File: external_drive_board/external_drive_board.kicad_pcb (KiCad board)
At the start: 2 copper layers, 90 x 90 mm, 26 parts, among them J1 MD-90SM, J2 MD-90SM, J3 Conn_02x17_Odd_Even, J4 Conn_01x04, J5 Conn_01x02, J6 Conn_01x02, J7 Conn_01x02, SW1 SW_DIP_x04, U1 74LS125, U2 74LS85, U3 74LS595, U4 74LS165, U5 74LS04

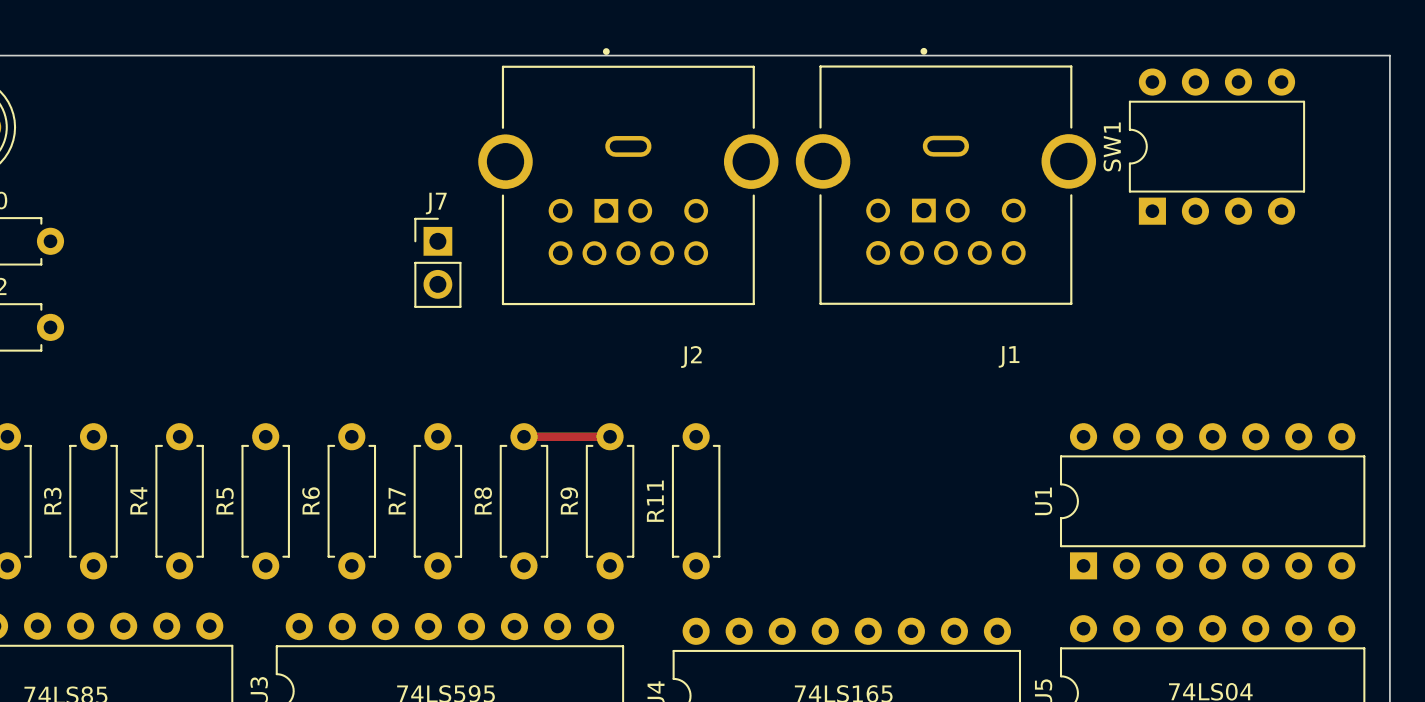
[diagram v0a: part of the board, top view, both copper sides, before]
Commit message: add dipsw reading to M1565 via spare bit
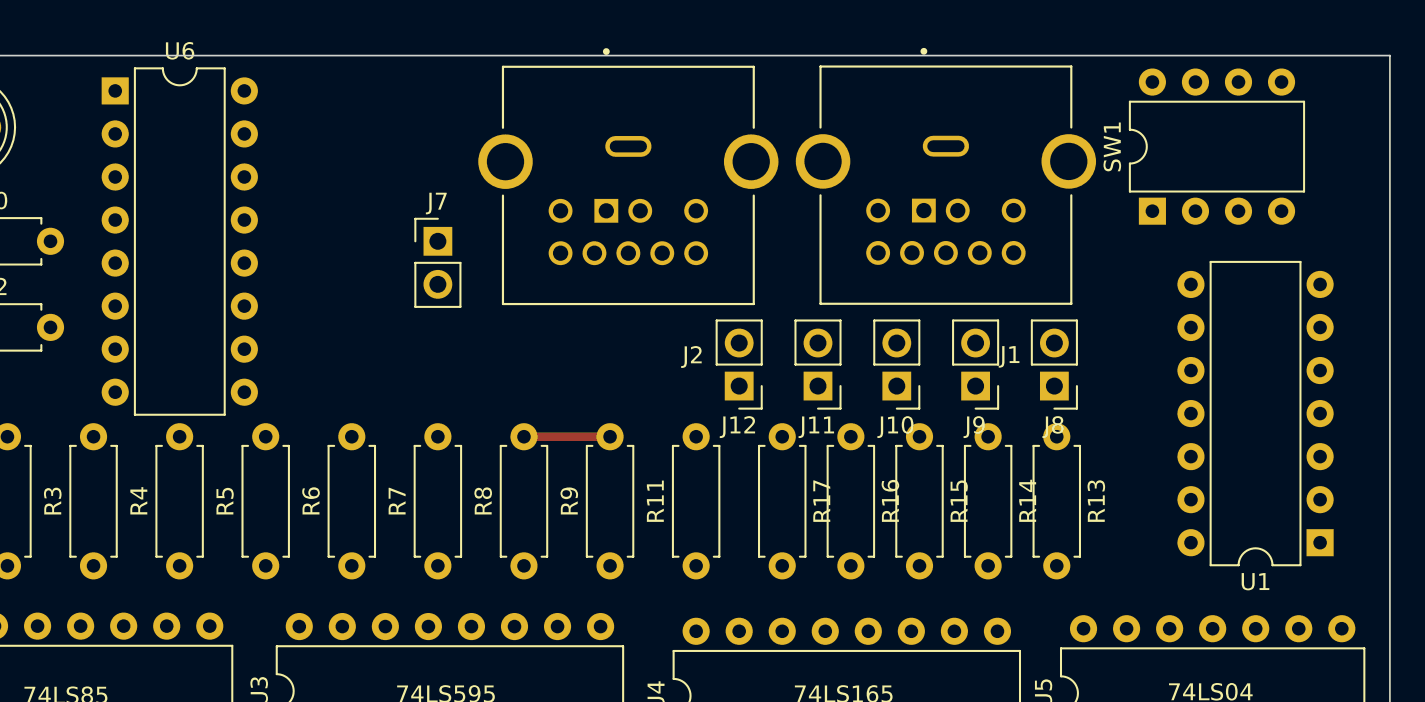
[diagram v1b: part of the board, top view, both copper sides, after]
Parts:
- added J10: RESERVED2, Connector_PinHeader_2.54mm:PinHeader_1x02_P2.54mm_Vertical, F.Cu at (110.9, 69.5)
- added J11: HD Drive, Connector_PinHeader_2.54mm:PinHeader_1x02_P2.54mm_Vertical, F.Cu at (106.2, 69.5)
- added J12: 5.25" Drive, Connector_PinHeader_2.54mm:PinHeader_1x02_P2.54mm_Vertical, F.Cu at (101.6, 69.5)
- added J8: RESERVED1, Connector_PinHeader_2.54mm:PinHeader_1x02_P2.54mm_Vertical, F.Cu at (120.2, 69.5)
- added J9: RESERVED3, Connector_PinHeader_2.54mm:PinHeader_1x02_P2.54mm_Vertical, F.Cu at (115.5, 69.5)
- added R13: 3K3, Resistor_THT:R_Axial_DIN0207_L6.3mm_D2.5mm_P7.62mm_Horizontal, F.Cu at (120.3, 72.5)
- added R14: 3K3, Resistor_THT:R_Axial_DIN0207_L6.3mm_D2.5mm_P7.62mm_Horizontal, F.Cu at (116.3, 72.5)
- added R15: 3K3, Resistor_THT:R_Axial_DIN0207_L6.3mm_D2.5mm_P7.62mm_Horizontal, F.Cu at (112.2, 72.5)
- added R16: 3K3, Resistor_THT:R_Axial_DIN0207_L6.3mm_D2.5mm_P7.62mm_Horizontal, F.Cu at (108.2, 72.5)
- added R17: 3K3, Resistor_THT:R_Axial_DIN0207_L6.3mm_D2.5mm_P7.62mm_Horizontal, F.Cu at (104.1, 72.5)
- added U6: 74LS165, Package_DIP:DIP-16_W7.62mm, F.Cu at (64.8, 52.1)
- moved U1 14.0 mm to (135.9, 78.7), turned to 180 degrees
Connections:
- U4 pad 6: SPR_SPARE -> M1565_DAT

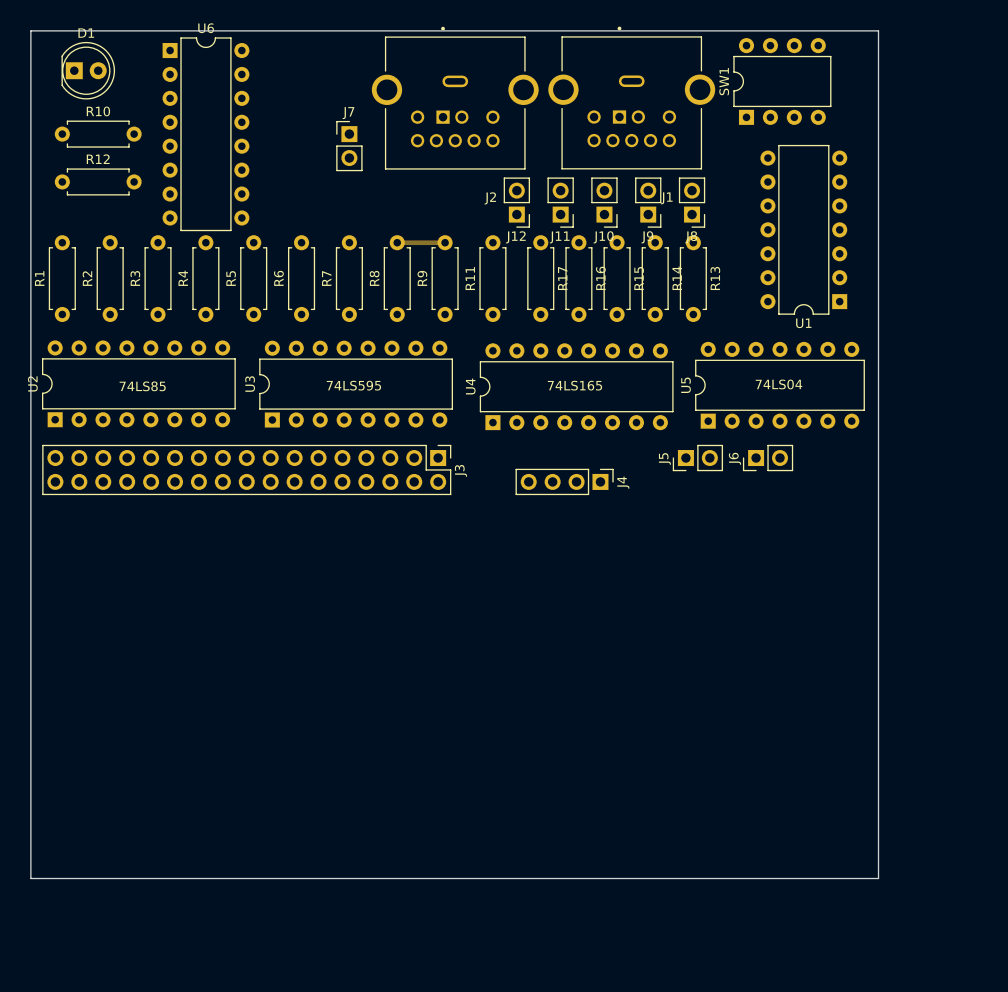
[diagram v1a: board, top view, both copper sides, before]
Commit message: route +5V and GND on M1565 board
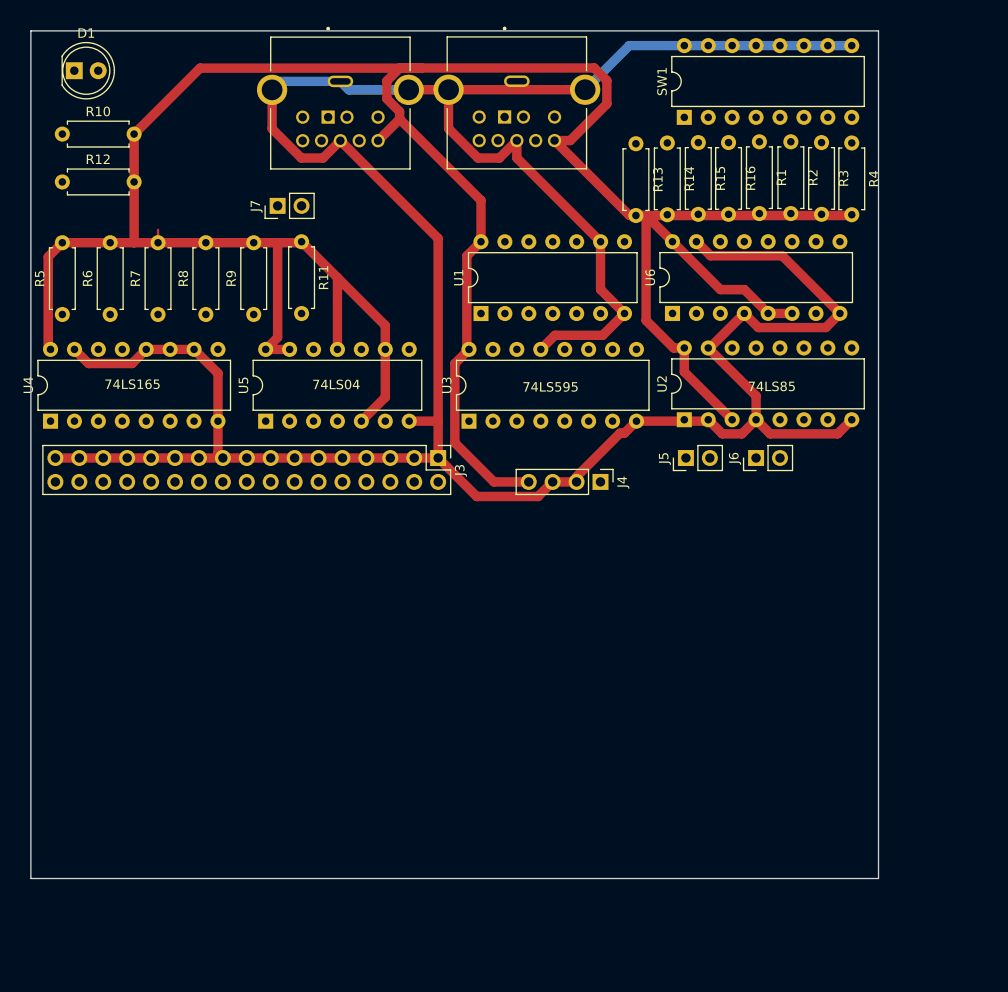
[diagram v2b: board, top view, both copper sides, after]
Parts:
- removed J10: RESERVED2, Connector_PinHeader_2.54mm:PinHeader_1x02_P2.54mm_Vertical
- removed J11: HD Drive, Connector_PinHeader_2.54mm:PinHeader_1x02_P2.54mm_Vertical
- removed J12: 5.25" Drive, Connector_PinHeader_2.54mm:PinHeader_1x02_P2.54mm_Vertical
- removed J8: RESERVED1, Connector_PinHeader_2.54mm:PinHeader_1x02_P2.54mm_Vertical
- removed J9: RESERVED3, Connector_PinHeader_2.54mm:PinHeader_1x02_P2.54mm_Vertical
- removed R17: 3K3, Resistor_THT:R_Axial_DIN0207_L6.3mm_D2.5mm_P7.62mm_Horizontal
- SW1: footprint Package_DIP:DIP-8_W7.62mm -> Package_DIP:DIP-16_W7.62mm
- moved R1 76.3 mm to (127.4, 61.8), turned to -90 degrees
- moved R2 74.6 mm to (130.7, 61.8), turned to -90 degrees
- moved R3 72.8 mm to (134.0, 61.9), turned to -90 degrees
- moved R4 71.0 mm to (137.2, 61.9), turned to -90 degrees
- moved U2 66.8 mm to (119.4, 91.3)
- moved U6 60.2 mm to (118.1, 80.0), turned to 90 degrees
- moved U5 47.0 mm to (74.9, 91.4)
- moved U4 47.0 mm to (52.1, 91.4)
- moved U1 38.1 mm to (97.8, 80.0), turned to 90 degrees
- moved R11 21.7 mm to (78.7, 72.4), turned to -90 degrees
- moved U3 20.9 mm to (96.5, 91.4)
- moved R8 20.3 mm to (68.6, 80.1)
- moved R9 20.3 mm to (73.7, 80.1)
- moved R5 20.3 mm to (53.3, 80.1)
- moved R6 20.3 mm to (58.4, 80.1)
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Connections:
- R13 pad 1: Net-(J9-Pin_2) -> DRIVE_5.25
- R14 pad 1: Net-(J8-Pin_2) -> DRIVE_HD
- R15 pad 1: Net-(J11-Pin_2) -> DIPSW3
- R16 pad 1: Net-(J12-Pin_1) -> DIPSW4
- SW1 pad 1: DRIVE_ID0 -> DRIVE_5.25
- SW1 pad 2: DRIVE_ID1 -> DRIVE_HD
- SW1 pad 3: DRIVE_ID2 -> DIPSW3
- SW1 pad 4: WRITE_EN -> DIPSW4
- SW1 pad 5: GND -> DRIVE_ID0
- SW1 pad 6: GND -> DRIVE_ID1
- SW1 pad 7: GND -> DRIVE_ID2
- SW1 pad 8: unconnected-(SW1-Pad8) -> WRITE_EN
- U6 pad 11: Net-(J10-Pin_2) -> unconnected-(U6-D0-Pad11)
- U6 pad 12: Net-(J9-Pin_2) -> DIPSW4
- U6 pad 13: Net-(J8-Pin_2) -> DIPSW3
- U6 pad 14: Net-(J11-Pin_2) -> DRIVE_HD
- U6 pad 3: Net-(J12-Pin_1) -> DRIVE_5.25
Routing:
- net GND: track 0.00 -> 329.8 mm
- net +5V: track 5.08 -> 302.3 mm

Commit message: more routing
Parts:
- moved J6 77.8 mm to (53.6, 69.5)
- moved J5 39.3 mm to (87.6, 72.4), turned to -90 degrees
- moved D1 1.33 mm to (55.9, 54.6), turned to 180 degrees
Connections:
- net FL_RDATA renamed F_RDATA_GATED
- J1 pad 3: FL_WDATA -> F_WDATA
- J1 pad 4: FL_WGATE -> F_WGATE
- J2 pad 3: FL_WDATA -> F_WDATA
- J2 pad 4: FL_WGATE -> F_WGATE
- U2 pad 10: DRIVE_ID0 -> DRIVE_ID2
- U2 pad 13: DRIVE_ID2 -> DRIVE_ID0
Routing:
- net M1565_DAT: track 0.00 -> 136.1 mm
- net 1565_CLK: track 0.00 -> 115.8 mm, vias 0 -> 9
- net F_WGATE: track 0.00 -> 78.7 mm
- net Net-(D1-K): track 0.00 -> 75.6 mm, vias 0 -> 1
- net F_WDATA: track 0.00 -> 67.9 mm, vias 0 -> 2
- net F_INDEX: track 0.00 -> 62.9 mm
- net F_DISKCHG: track 0.00 -> 56.8 mm, vias 0 -> 2
- net F_SIDE: track 0.00 -> 51.7 mm, vias 0 -> 2
- net DRIVE_ID0: track 0.00 -> 50.5 mm
- net F_RDATA: track 0.00 -> 43.3 mm, vias 0 -> 5
- net DRIVE_ID1: track 0.00 -> 40.7 mm
- net LD_N: track 0.00 -> 36.2 mm, vias 0 -> 1
- net 1565_LD_5V: track 0.00 -> 29.5 mm, vias 0 -> 2
- net DRIVE_5.25: track 0.00 -> 29.1 mm, vias 0 -> 1
- net DRIVE_ID2: track 0.00 -> 28.1 mm
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
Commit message: more work on M1565 board
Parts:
- removed J6: Conn_01x02, Connector_PinHeader_2.54mm:PinHeader_1x02_P2.54mm_Vertical
- added H1: MountingHole, MountingHole:MountingHole_3mm_Pad, F.Cu at (66.0, 55.9)
- added H2: MountingHole, MountingHole:MountingHole_3mm_Pad, F.Cu at (55.9, 106.7)
- added H3: MountingHole, MountingHole:MountingHole_3mm_Pad, F.Cu at (132.1, 106.7)
- J5, J7: value Conn_01x02 -> Conn_01x03; footprint Connector_PinHeader_2.54mm:PinHeader_1x02_P2.54mm_Vertical -> Connector_PinHeader_2.54mm:PinHeader_1x03_P2.54mm_Vertical
- moved J7 22.6 mm to (53.6, 69.6)
- moved J5 15.7 mm to (72.4, 68.6), turned to 90 degrees
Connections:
- J3 pad 12: F_DRVSB -> C1565_SELECTED_N
- J3 pad 14: F_DRVSA -> C1565_SELECTED_N
- J3 pad 16: F_MOTEB -> F_MOTEA
- J5 pad 1: Net-(J5-Pin_1) -> LD_N
- J5 pad 2: LD_N -> Net-(J5-Pin_2)
- J7 pad 1: 1565_LD_5V -> LD_N
- J7 pad 2: unconnected-(J7-Pin_2-Pad2) -> Net-(J7-Pin_2)
- U3 pad 12: Net-(J5-Pin_1) -> Net-(J5-Pin_2)
- U3 pad 6: F_MOTOR -> F_MOTEA
- U4 pad 1: Net-(J6-Pin_1) -> Net-(J7-Pin_2)
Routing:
- net 1565_LD_5V: track 29.5 -> 87.7 mm, vias 2 -> 7
- net C1565_SELECTED: track 0.00 -> 56.7 mm, vias 0 -> 2
- net C1565_SELECTED_N: track 0.00 -> 43.6 mm, vias 0 -> 2
- net 1565_RST: track 20.1 -> 62.5 mm, vias 0 -> 1
- net F_STEP: track 0.00 -> 42.0 mm, vias 0 -> 3
- net Net-(J5-Pin_2): track 0.00 -> 41.2 mm, vias 0 -> 2
- net DRIVE_SEL0: track 0.00 -> 40.6 mm, vias 0 -> 1
- net DRIVE_SEL2: track 0.00 -> 40.5 mm, vias 0 -> 1
- net SERIO_O: track 0.00 -> 39.7 mm
- net DRIVE_SEL1: track 0.00 -> 38.8 mm
- net F_MOTEA: track 0.00 -> 37.5 mm, vias 0 -> 2
- net SERIO_GATE: track 0.00 -> 37.3 mm, vias 0 -> 1
- net F_STEPDIR: track 0.00 -> 36.5 mm, vias 0 -> 2
- net /SERIO_5V: track 25.9 -> 62.2 mm, vias 1 -> 2
- net F_LED: track 0.00 -> 34.4 mm, vias 0 -> 2
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
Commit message: more work on external drive board
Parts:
- SW1: value SW_DIP_x04 -> SW_DIP_x08
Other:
- board text added: "5V"
- board text added: "GND"
- board text added: "NC"
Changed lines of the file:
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@@
         (effects (font (size 1 1) (thickness 0.15)))
     )
-    (fp_text value "74LS125" (at 3.81 17.57 90) (layer "F.Fab")
+    (fp_text value "74LS125" (at 3.81 6.35 180) (layer "F.SilkS")
         (effects (font (size 1 1) (thickness 0.15)))
     )
@@
         (effects (font (size 1 1) (thickness 0.15)))
     )
-    (fp_text value "SW_DIP_x04" (at 3.81 20.11 90) (layer "F.Fab")
+    (fp_text value "SW_DIP_x08" (at 3.777962 8.662302 180) (layer "F.SilkS")
         (effects (font (size 1 1) (thickness 0.15)))
     )
@@
         (effects (font (size 1 1) (thickness 0.15)))
     )
-    (fp_text value "74LS165" (at 3.81 20.11 90) (layer "F.Fab")
+    (fp_text value "74LS165" (at 3.81 8.875 180) (layer "F.SilkS")
         (effects (font (size 1 1) (thickness 0.15)))
     )
@@
   (gr_rect (start 50 50) (end 140 140)
     (stroke (width 0.1) (type default)) (fill none) (layer "Edge.Cuts"))
+  (gr_text "NC" (at 109.179071 95.741634) (layer "B.SilkS")
+    (effects (font (size 1.5 1.5) (thickness 0.3) bold) (justify left bottom))
+  )
+  (gr_text "GND" (at 104.194636 96.117174) (layer "B.SilkS")
+    (effects (font (size 1.5 1.5) (thickness 0.3) bold) (justify left bottom))
+  )
+  (gr_text "5V" (at 101.36102 95.844054) (layer "F.SilkS")
+    (effects (font (size 1.5 1.5) (thickness 0.3) bold) (justify left bottom))
+  )
   (segment (start 91.44 91.44) (end 91.44 93.5482) (width 1) (layer "F.Cu") (net 1))
   (segment (start 56.125 85.32) (end 54.625 83.82) (width 1) (layer "F.Cu") (net 1))

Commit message: finish M1565 initial board rev
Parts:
- added H4: MountingHole, MountingHole:MountingHole_3mm_Pad, F.Cu at (147.0, 55.0)
- SW1: value SW_DIP_x08 -> SW_DIP_x04
- moved H3 41.1 mm to (147.0, 145.0)
- moved H2 38.4 mm to (53.0, 145.0)
- moved H1 13.1 mm to (53.0, 55.0)
- moved D1 12.2 mm to (68.1, 55.4)
- moved R2 0.68 mm to (131.3, 61.5)
- moved R4 0.68 mm to (137.8, 61.6)
- moved J3 0.68 mm to (93.9, 95.1)
- moved R1 0.68 mm to (128.0, 61.5)
- moved R14 0.68 mm to (118.2, 61.6)
- moved SW1 0.68 mm to (120.0, 58.9)
- moved J1 0.68 mm to (102.2, 55.1)
- moved J2 0.68 mm to (83.5, 55.1)
- moved J4 0.68 mm to (111.1, 97.6)
- moved J5 0.68 mm to (73.0, 68.3)
- moved J7 0.68 mm to (54.2, 69.3)
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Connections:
- net DIPSW3 renamed DENSITY1
- net DRIVE_HD renamed DENSITY0
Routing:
- net Net-(D1-K): track 77.5 -> 64.5 mm
- net Net-(D1-A): track 11.4 -> 18.9 mm
- added copper zone on B.Cu, net GND
- added copper zone on F.Cu, net GND
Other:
- board size 90 x 90 mm -> 100 x 100 mm
- board text added: "DIP Switches: (SW1) 3.5/5.25{dblquote} DENSITY0 DENSITY1 -RESERVED- DRV ID 0 DRV ID 1 DRV ID 2 WRIT PROT (Hole H4) Densities: 00 = DD (720/320KB) 01 = HD (1.2/1.44MB) 10 = QD (1M 5.25{dblquote}) 11 = ED (2.88MB)"
- board text added: "If you can read this text you have probably lost your floppy drive"
- board text added: "MEGA65 M1565 Controller Board revA (C) Paul Gardner-Stephen 2024 CC-BY-SA-4.0"
- board text added: "The floppy drive goes on the other side."
